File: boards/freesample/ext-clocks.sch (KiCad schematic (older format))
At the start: 45 parts, among them J3 SMA, J4 SMA, J5 SMA, U1 HMC675LP3E, U2 HMC675LP3E, U3 PI6C59S6005

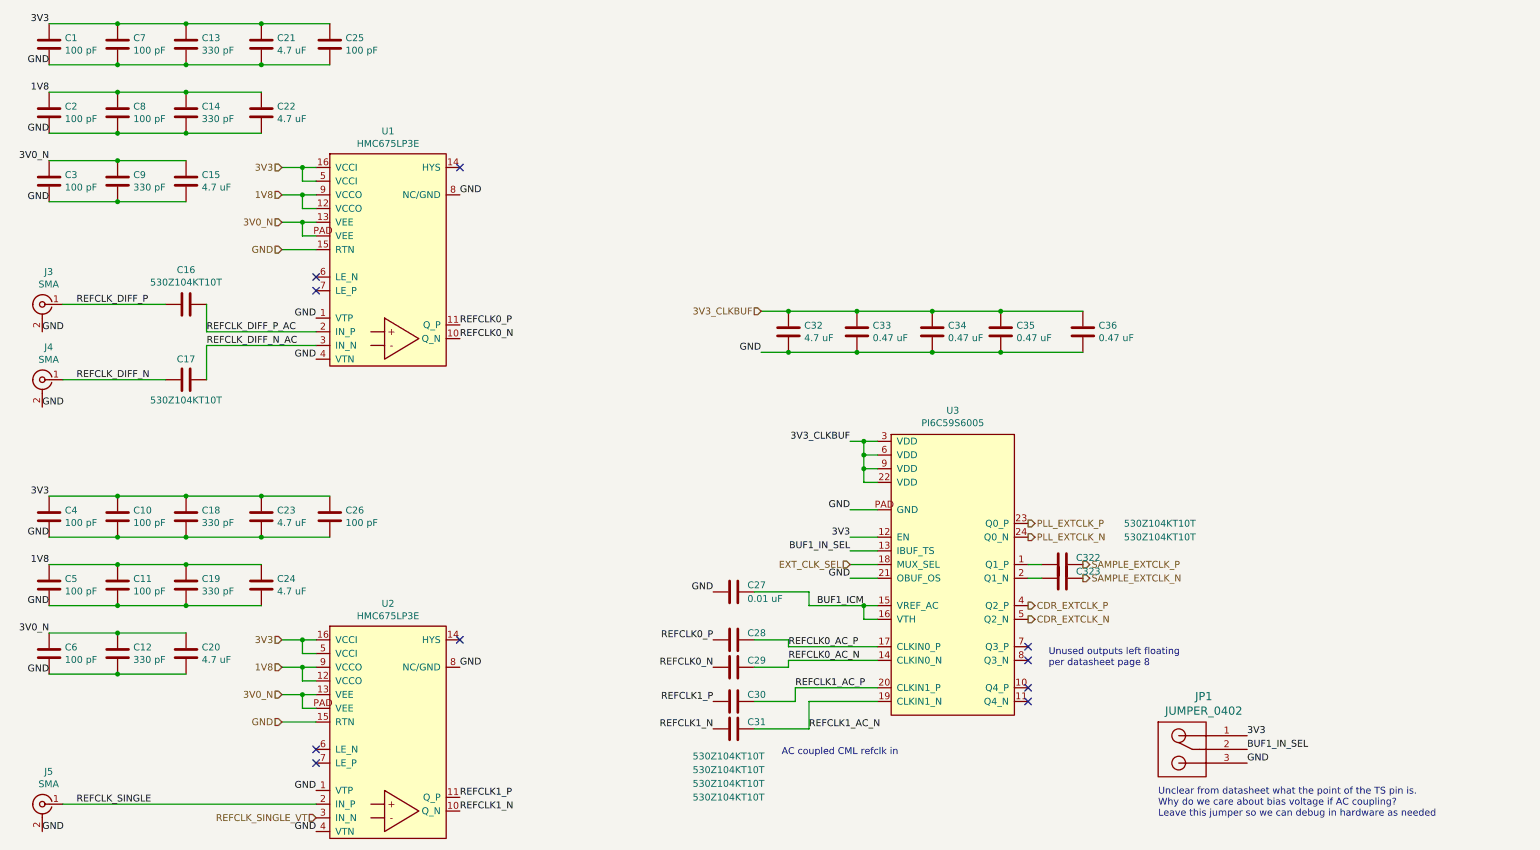
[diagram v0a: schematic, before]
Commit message: Added more test points. Started picking packages for passives. Continued schematic review.
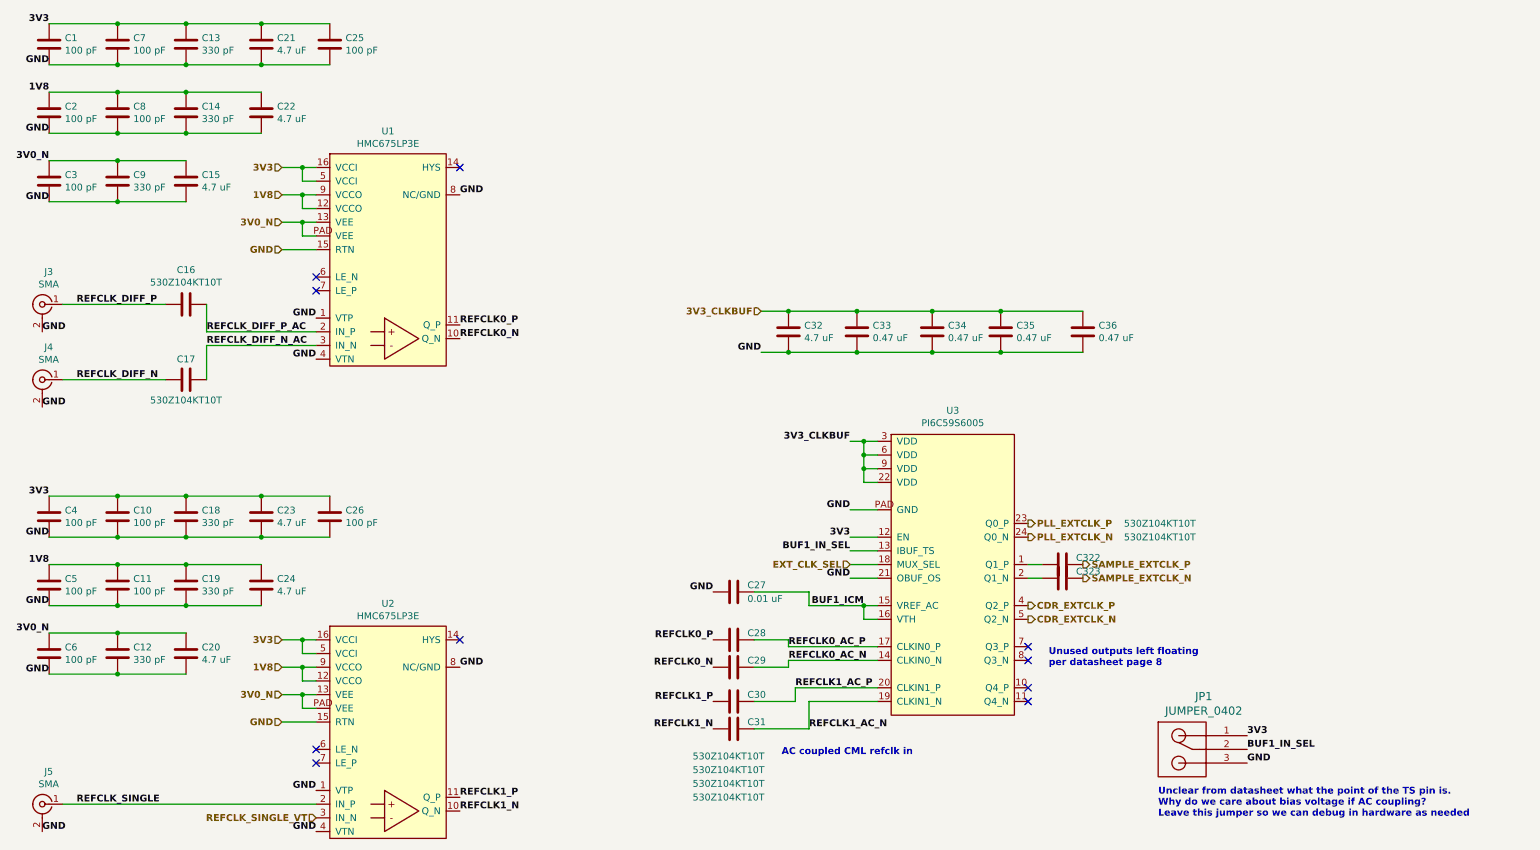
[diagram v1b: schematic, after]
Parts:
- C1, C10, C11, C12, C13, C14, C16, C17, C18, C19, C2, C25, C26, C28, C29, C3, C30, C31, C322, C323, C4, C5, C6, C7, C8, C9: footprint (none) -> azonenberg_pcb:EIA_0201_CAP_NOSILK
- C15, C20, C21, C22, C23, C24, C32: footprint (none) -> azonenberg_pcb:EIA_0603_CAP_NOSILK
- C27, C33, C34, C35, C36: footprint (none) -> azonenberg_pcb:EIA_0402_CAP_NOSILK
- J3, J4, J5: footprint (none) -> azonenberg_pcb:CONN_SMA_EDGE_SAMTEC_SMA_J_P_H_ST_EM1
- JP1: footprint (none) -> azonenberg_pcb:EIA_0402_JUMPER
- U1, U2: footprint (none) -> azonenberg_pcb:QFN_16_0.5MM_3x3MM
- U3: footprint (none) -> azonenberg_pcb:QFN_24_0.5MM_4x4MM

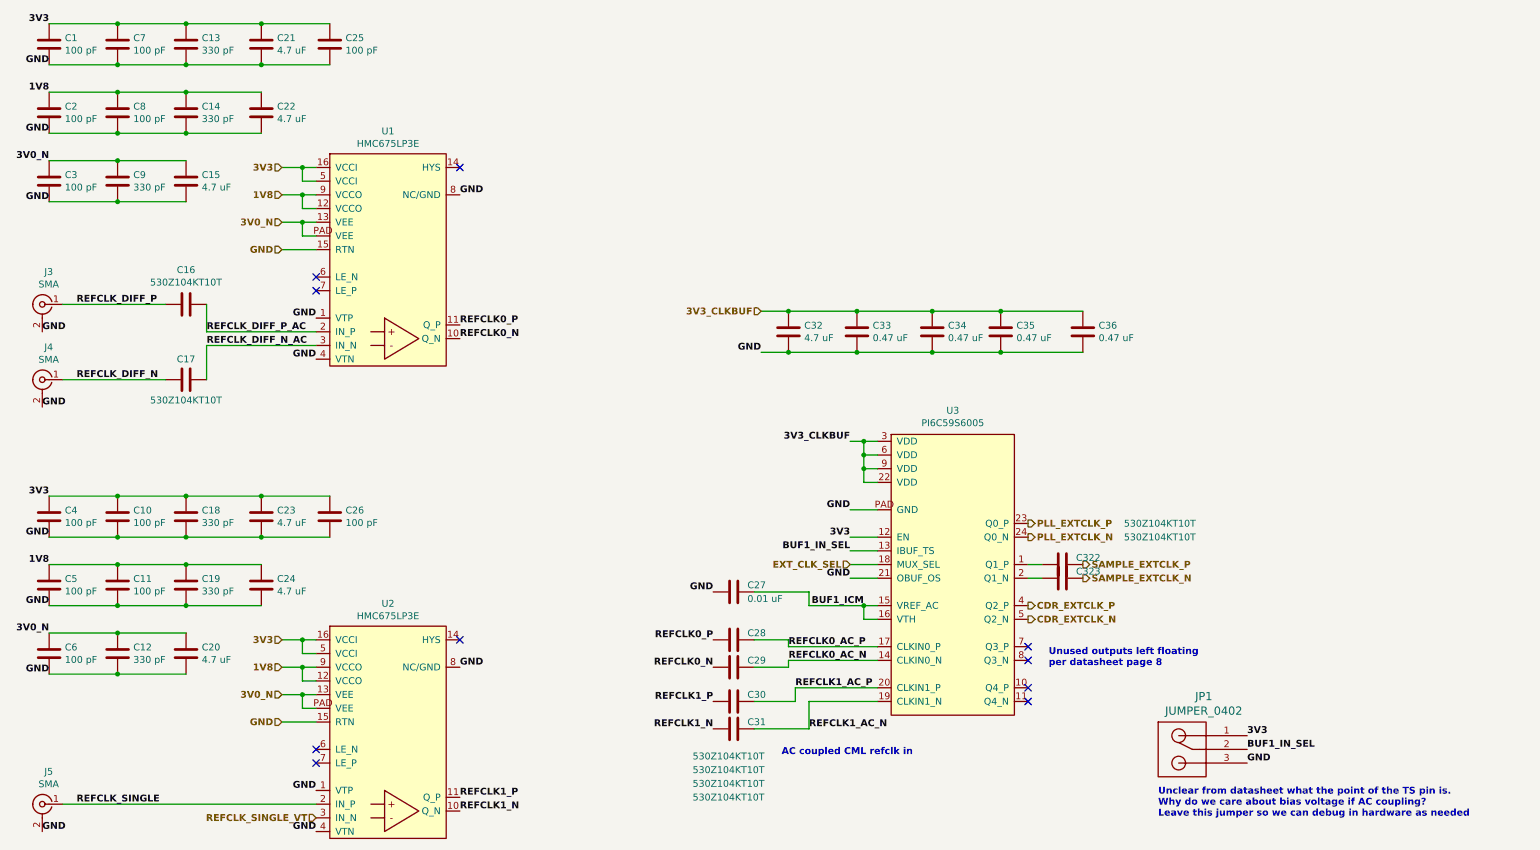
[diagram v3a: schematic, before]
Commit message: Initial layout of external refclks block
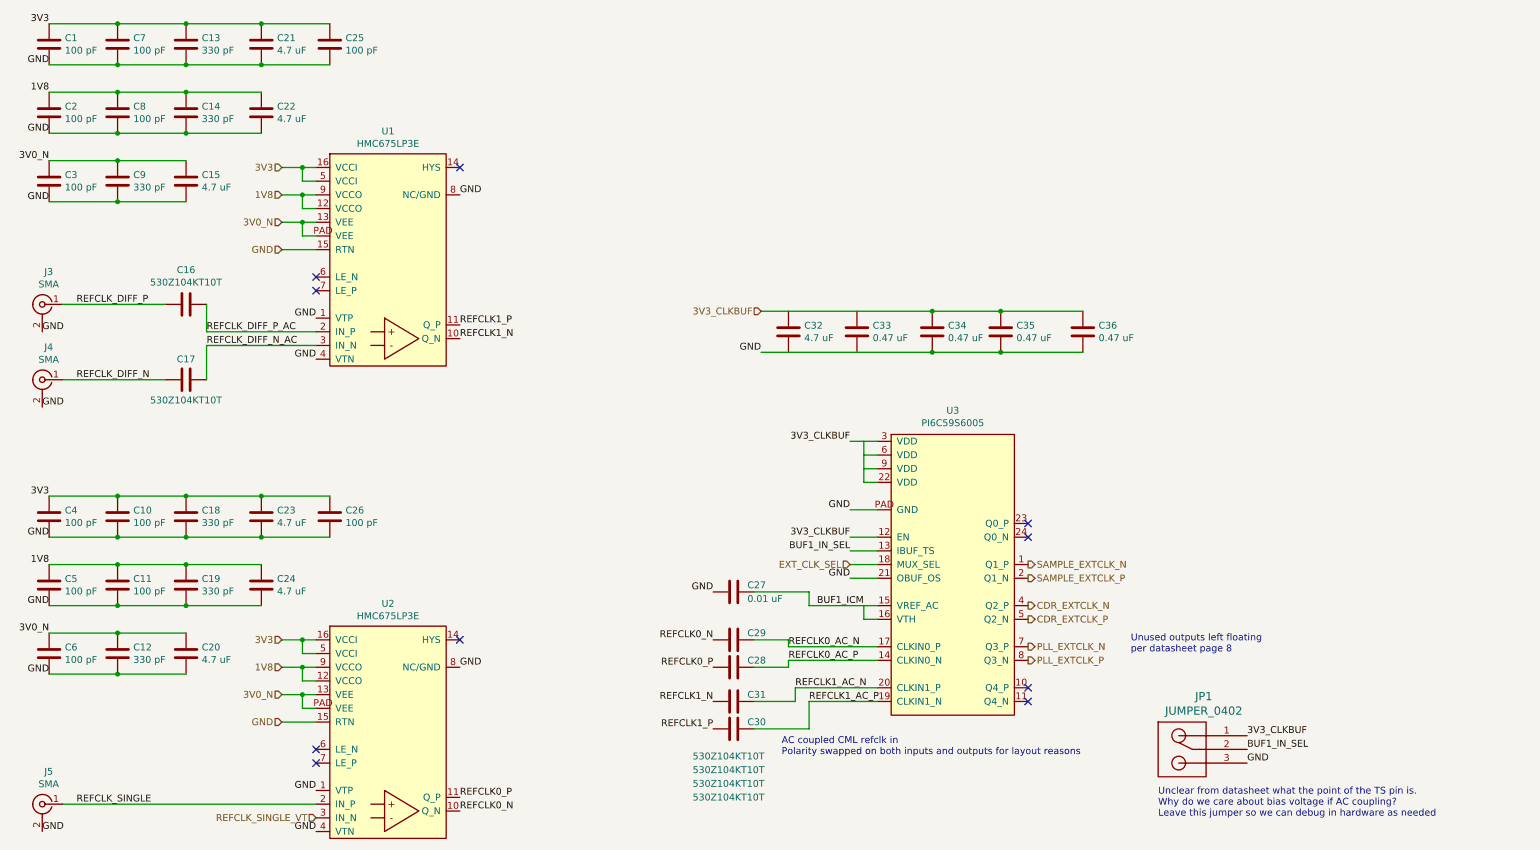
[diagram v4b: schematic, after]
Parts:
- removed C322, C323: 530Z104KT10T, azonenberg_pcb:EIA_0201_CAP_NOSILK, symbol device:C
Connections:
- net 3V3: no longer JP1.1, U3.12 (EN)
- net 3V3_CLKBUF: now also JP1.1, U3.12 (EN)
- net CDR_EXTCLK_N: now also U3.4 (Q2_P); no longer U3.5 (Q2_N)
- net CDR_EXTCLK_P: now also U3.5 (Q2_N); no longer U3.4 (Q2_P)
- net PLL_EXTCLK_N: now also U3.7 (Q3_P); no longer U3.24 (Q0_N)
- net PLL_EXTCLK_P: now also U3.8 (Q3_N); no longer U3.23 (Q0_P)
- net REFCLK0_AC_N: now also U3.17 (CLKIN0_P); no longer U3.14 (CLKIN0_N)
- net REFCLK0_AC_P: now also U3.14 (CLKIN0_N); no longer U3.17 (CLKIN0_P)
- net REFCLK0_N: now also U2.10 (Q_N); no longer U1.10 (Q_N)
- net REFCLK0_P: now also U2.11 (Q_P); no longer U1.11 (Q_P)
- net REFCLK1_AC_N: now also U3.20 (CLKIN1_P); no longer U3.19 (CLKIN1_N)
- net REFCLK1_AC_P: now also U3.19 (CLKIN1_N); no longer U3.20 (CLKIN1_P)
- net REFCLK1_N: now also U1.10 (Q_N); no longer U2.10 (Q_N)
- net REFCLK1_P: now also U1.11 (Q_P); no longer U2.11 (Q_P)
- net SAMPLE_EXTCLK_N: now also U3.1 (Q1_P)
- net SAMPLE_EXTCLK_P: now also U3.2 (Q1_N)
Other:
- note added: "AC coupled CML refclk in\nPolarity swapped on both inputs and outputs for layout reasons"
- note removed: "AC coupled CML refclk in"
- moved on the sheet: C28, C29, C30, C31

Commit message: Began layout on clock recovery block
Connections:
- net CDR_EXTCLK_N: now also U3.7 (Q3_P); no longer U3.4 (Q2_P)
- net CDR_EXTCLK_P: now also U3.8 (Q3_N); no longer U3.5 (Q2_N)
- net PLL_EXTCLK_N: now also U3.4 (Q2_P); no longer U3.7 (Q3_P)
- net PLL_EXTCLK_P: now also U3.5 (Q2_N); no longer U3.8 (Q3_N)
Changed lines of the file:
@@
 Comp "Andrew D. Zonenberg / Antikernel Labs"
 Comment1 "External reference clocks"
-Comment2 "Layout in progress"
+Comment2 "Initial layout complete"
 Comment3 ""
 Comment4 ""
@@
 Text HLabel 6600 4600 0    50   Input ~ 0
 EXT_CLK_SEL
-Text HLabel 7900 5300 2    50   Output ~ 0
+Text HLabel 7900 5000 2    50   Output ~ 0
 PLL_EXTCLK_P
-Text HLabel 7900 5200 2    50   Output ~ 0
+Text HLabel 7900 4900 2    50   Output ~ 0
 PLL_EXTCLK_N
 $Comp
@@
 Text Notes 8850 6450 0    50   ~ 0
 Unclear from datasheet what the point of the TS pin is.\nWhy do we care about bias voltage if AC coupling?\nLeave this jumper so we can debug in hardware as needed
-Text HLabel 7900 5000 2    50   Output ~ 0
+Text HLabel 7900 5300 2    50   Output ~ 0
 CDR_EXTCLK_P
-Text HLabel 7900 4900 2    50   Output ~ 0
+Text HLabel 7900 5200 2    50   Output ~ 0
 CDR_EXTCLK_N
 Text HLabel 5950 2750 0    50   Input ~ 0

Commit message: Moved CDR block down so it's closer to the level trigger
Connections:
- net CDR_EXTCLK_N: now also U3.4 (Q2_P); no longer U3.7 (Q3_P)
- net CDR_EXTCLK_P: now also U3.5 (Q2_N); no longer U3.8 (Q3_N)
- net PLL_EXTCLK_N: now also U3.7 (Q3_P); no longer U3.4 (Q2_P)
- net PLL_EXTCLK_P: now also U3.8 (Q3_N); no longer U3.5 (Q2_N)
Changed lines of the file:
@@
 Sheet 2 12
 Title "FREESAMPLE Oscilloscope"
-Date "2019-03-19"
+Date "2019-03-20"
 Rev "0.1"
 Comp "Andrew D. Zonenberg / Antikernel Labs"
@@
 Text HLabel 6600 4600 0    50   Input ~ 0
 EXT_CLK_SEL
-Text HLabel 7900 5000 2    50   Output ~ 0
+Text HLabel 7900 5300 2    50   Output ~ 0
 PLL_EXTCLK_P
-Text HLabel 7900 4900 2    50   Output ~ 0
+Text HLabel 7900 5200 2    50   Output ~ 0
 PLL_EXTCLK_N
 $Comp
@@
 Text Notes 8850 6450 0    50   ~ 0
 Unclear from datasheet what the point of the TS pin is.\nWhy do we care about bias voltage if AC coupling?\nLeave this jumper so we can debug in hardware as needed
-Text HLabel 7900 5300 2    50   Output ~ 0
+Text HLabel 7900 5000 2    50   Output ~ 0
 CDR_EXTCLK_P
-Text HLabel 7900 5200 2    50   Output ~ 0
+Text HLabel 7900 4900 2    50   Output ~ 0
 CDR_EXTCLK_N
 Text HLabel 5950 2750 0    50   Input ~ 0

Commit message: Tweaks to PLL and CDR layout, swapped a few signals around. Began work on level trigger and ADC layout.
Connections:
- net SAMPLE_EXTCLK_N: now also U3.10 (Q4_P); no longer U3.1 (Q1_P)
- net SAMPLE_EXTCLK_P: now also U3.11 (Q4_N); no longer U3.2 (Q1_N)
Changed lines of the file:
@@
 Wire Wire Line
 	6600 4600 6800 4600
-Text HLabel 7900 4700 2    50   Output ~ 0
+Text HLabel 7900 5600 2    50   Output ~ 0
 SAMPLE_EXTCLK_P
-Text HLabel 7900 4600 2    50   Output ~ 0
+Text HLabel 7900 5500 2    50   Output ~ 0
 SAMPLE_EXTCLK_N
-NoConn ~ 7900 5500
-NoConn ~ 7900 5600
 Text Notes 8650 5250 0    50   ~ 0
 Unused outputs left floating\nper datasheet page 8
@@
 NoConn ~ 7900 4400
 NoConn ~ 7900 4300
+NoConn ~ 7900 4700
+NoConn ~ 7900 4600
 $EndSCHEMATC
